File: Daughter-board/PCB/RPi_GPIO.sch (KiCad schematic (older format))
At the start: 15 parts, among them J1 Conn_01x05, J2 RPi_GPIO, J3 Conn_01x05, J4 Conn_01x05, J5 Conn_01x07, J6 Conn_01x07, J7 Conn_01x05, J8 Conn_02x07_Odd_Even, J9 Conn_01x04, Q1 2N7002, Q2 2N7002, Q3 2N7002

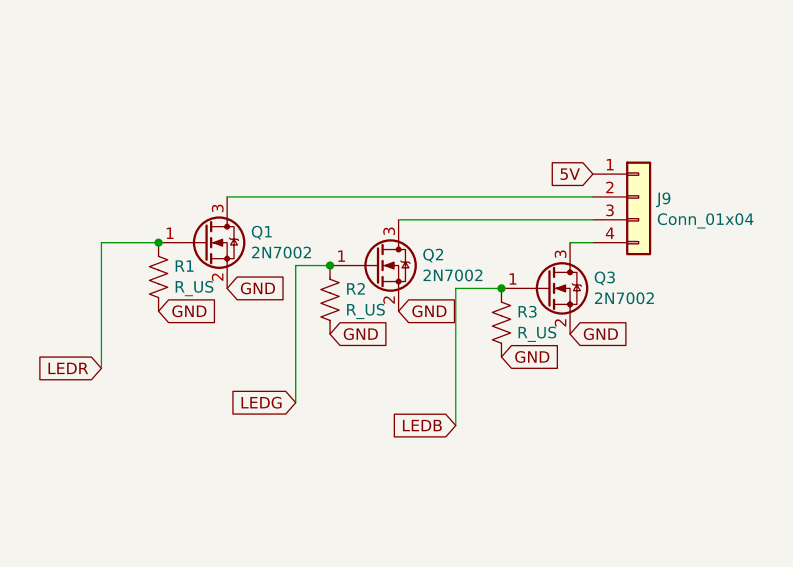
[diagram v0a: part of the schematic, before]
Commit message: smt to TH
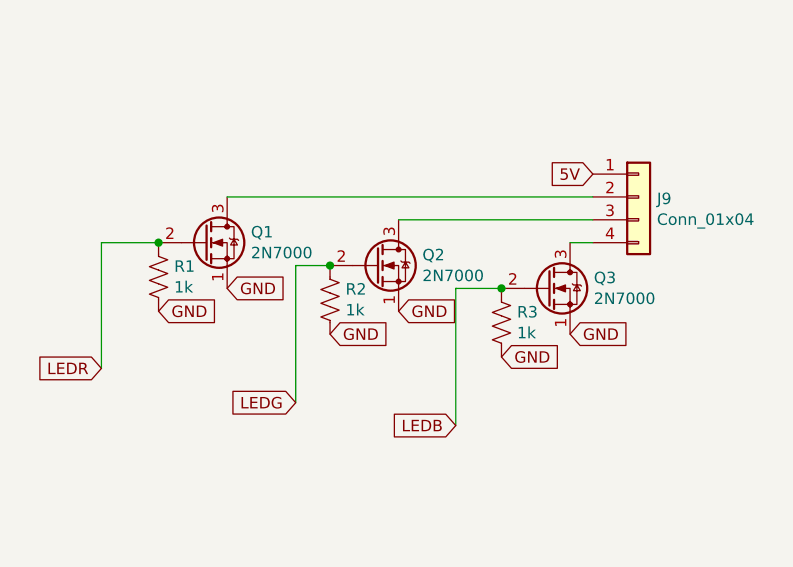
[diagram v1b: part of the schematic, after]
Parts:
- removed Q1, Q2, Q3: 2N7002, Package_TO_SOT_SMD:SOT-23, symbol Transistor_FET:2N7002
- added Q1, Q2, Q3: 2N7000, Package_TO_SOT_THT:TO-92_Inline, symbol Transistor_FET:2N7000
- J2: footprint RPi_Hat:Pin_Header_Straight_2x20 -> cidco:Pin_Header_Straight_2x20
- R1, R2, R3: value R_US -> 1k; footprint Resistor_SMD:R_0805_2012Metric -> Resistor_THT:R_Axial_DIN0207_L6.3mm_D2.5mm_P10.16mm_Horizontal
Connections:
- net GND: now also Q1.1 (S), Q2.1 (S), Q3.1 (S)
- net LEDB: now also Q3.2 (G)
- net LEDG: now also Q2.2 (G)
- net LEDR: now also Q1.2 (G)
- net at J9.2 (Pin_2): now also Q1.3 (D)
- net at J9.3 (Pin_3): now also Q2.3 (D)
- net at J9.4 (Pin_4): now also Q3.3 (D)
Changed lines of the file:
@@
 F 0 "J2" H 5900 3000 60  0000 C CNN
 F 1 "RPi_GPIO" H 5900 2900 60  0000 C CNN
-F 2 "RPi_Hat:Pin_Header_Straight_2x20" H 5150 2750 60  0001 C CNN
+F 2 "cidco:Pin_Header_Straight_2x20" H 5150 2750 60  0001 C CNN
 F 3 "" H 5150 2750 60  0000 C CNN
 	1    5150 2750
@@
 $EndComp
 $Comp
-L Transistor_FET:2N7002 Q2
-U 1 1 5E362224
-P 9150 2050
-F 0 "Q2" H 9354 2096 50  0000 L CNN
-F 1 "2N7002" H 9354 2005 50  0000 L CNN
-F 2 "Package_TO_SOT_SMD:SOT-23" H 9350 1975 50  0001 L CIN
-F 3 "https://www.fairchildsemi.com/datasheets/2N/2N7002.pdf" H 9150 2050 50  0001 L CNN
-	1    9150 2050
-	1    0    0    -1
-$EndComp
-$Comp
-L Transistor_FET:2N7002 Q1
-U 1 1 5E362E69
-P 8400 1950
-F 0 "Q1" H 8604 1996 50  0000 L CNN
-F 1 "2N7002" H 8604 1905 50  0000 L CNN
-F 2 "Package_TO_SOT_SMD:SOT-23" H 8600 1875 50  0001 L CIN
-F 3 "https://www.fairchildsemi.com/datasheets/2N/2N7002.pdf" H 8400 1950 50  0001 L CNN
-	1    8400 1950
-	1    0    0    -1
-$EndComp
-$Comp
 L device:R_US R1
 U 1 1 5E36419D
 P 8200 2100
 F 0 "R1" H 8268 2146 50  0000 L CNN
-F 1 "R_US" H 8268 2055 50  0000 L CNN
-F 2 "Resistor_SMD:R_0805_2012Metric" V 8240 2090 50  0001 C CNN
+F 1 "1k" H 8268 2055 50  0000 L CNN
+F 2 "Resistor_THT:R_Axial_DIN0207_L6.3mm_D2.5mm_P10.16mm_Horizontal" V 8240 2090 50  0001 C CNN
 F 3 "~" H 8200 2100 50  0001 C CNN
 	1    8200 2100
-	1    0    0    -1
-$EndComp
-$Comp
-L device:R_US R2
-U 1 1 5E364C8E
-P 8950 2200
-F 0 "R2" H 9018 2246 50  0000 L CNN
-F 1 "R_US" H 9018 2155 50  0000 L CNN
-F 2 "Resistor_SMD:R_0805_2012Metric" V 8990 2190 50  0001 C CNN
-F 3 "~" H 8950 2200 50  0001 C CNN
-	1    8950 2200
 	1    0    0    -1
 $EndComp
@@
 P 9700 2300
 F 0 "R3" H 9768 2346 50  0000 L CNN
-F 1 "R_US" H 9768 2255 50  0000 L CNN
-F 2 "Resistor_SMD:R_0805_2012Metric" V 9740 2290 50  0001 C CNN
+F 1 "1k" H 9768 2255 50  0000 L CNN
+F 2 "Resistor_THT:R_Axial_DIN0207_L6.3mm_D2.5mm_P10.16mm_Horizontal" V 9740 2290 50  0001 C CNN
 F 3 "~" H 9700 2300 50  0001 C CNN
 	1    9700 2300
@@
 Text GLabel 10100 1650 0    50   Input ~ 0
 5V
-$Comp
-L Transistor_FET:2N7002 Q3
-U 1 1 5E3665A2
-P 9900 2150
-F 0 "Q3" H 10104 2196 50  0000 L CNN
-F 1 "2N7002" H 10104 2105 50  0000 L CNN
-F 2 "Package_TO_SOT_SMD:SOT-23" H 10100 2075 50  0001 L CIN
-F 3 "https://www.fairchildsemi.com/datasheets/2N/2N7002.pdf" H 9900 2150 50  0001 L CNN
-	1    9900 2150
-	1    0    0    -1
-$EndComp
 Wire Wire Line
 	9250 1850 10100 1850
@@
 Wire Wire Line
 	7950 1950 7950 2500
+Wire Wire Line
+	8950 2050 8800 2050
+Wire Wire Line
+	9700 2150 9500 2150
+Wire Wire Line
+	9500 2150 9500 2750
+Wire Wire Line
+	8800 2050 8800 2650
+$Comp
+L device:R_US R2
+U 1 1 5E364C8E
+P 8950 2200
+F 0 "R2" H 9018 2246 50  0000 L CNN
+F 1 "1k" H 9018 2155 50  0000 L CNN
+F 2 "Resistor_THT:R_Axial_DIN0207_L6.3mm_D2.5mm_P10.16mm_Horizontal" V 8990 2190 50  0001 C CNN
+F 3 "~" H 8950 2200 50  0001 C CNN
+	1    8950 2200
+	1    0    0    -1
+$EndComp
+$Comp
+L Transistor_FET:2N7000 Q3
+U 1 1 5E653316
+P 9900 2150
+F 0 "Q3" H 10104 2196 50  0000 L CNN
+F 1 "2N7000" H 10104 2105 50  0000 L CNN
+F 2 "Package_TO_SOT_THT:TO-92_Inline" H 10100 2075 50  0001 L CIN
+F 3 "https://www.fairchildsemi.com/datasheets/2N/2N7000.pdf" H 9900 2150 50  0001 L CNN
+	1    9900 2150
+	1    0    0    -1
+$EndComp
+Connection ~ 9700 2150
+$Comp
+L Transistor_FET:2N7000 Q2
+U 1 1 5E653BFB
+P 9150 2050
+F 0 "Q2" H 9354 2096 50  0000 L CNN
+F 1 "2N7000" H 9354 2005 50  0000 L CNN
+F 2 "Package_TO_SOT_THT:TO-92_Inline" H 9350 1975 50  0001 L CIN
+F 3 "https://www.fairchildsemi.com/datasheets/2N/2N7000.pdf" H 9150 2050 50  0001 L CNN
+	1    9150 2050
+	1    0    0    -1
+$EndComp
+Connection ~ 8950 2050
+$Comp
+L Transistor_FET:2N7000 Q1
+U 1 1 5E6542F3
+P 8400 1950
+F 0 "Q1" H 8604 1996 50  0000 L CNN
+F 1 "2N7000" H 8604 1905 50  0000 L CNN
+F 2 "Package_TO_SOT_THT:TO-92_Inline" H 8600 1875 50  0001 L CIN
+F 3 "https://www.fairchildsemi.com/datasheets/2N/2N7000.pdf" H 8400 1950 50  0001 L CNN
+	1    8400 1950
+	1    0    0    -1
+$EndComp
 Connection ~ 8200 1950
-Wire Wire Line
-	8950 2050 8800 2050
-Wire Wire Line
-	8800 2050 8800 2650
-Connection ~ 8950 2050
-Wire Wire Line
-	9700 2150 9500 2150
-Wire Wire Line
-	9500 2150 9500 2750
-Connection ~ 9700 2150
 $EndSCHEMATC
